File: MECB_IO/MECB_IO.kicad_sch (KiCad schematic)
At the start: 37 parts, among them J1 MECB_64AC, J2 Conn_02x10_Odd_Even, J3 Conn_01x03, SW1 SW_DIP_x08, U1 ATF22V10C-15PU, U2 74LS174, U3 DS1302+, U4 74LS245, U5 74LS374, Y1 32.768kHz

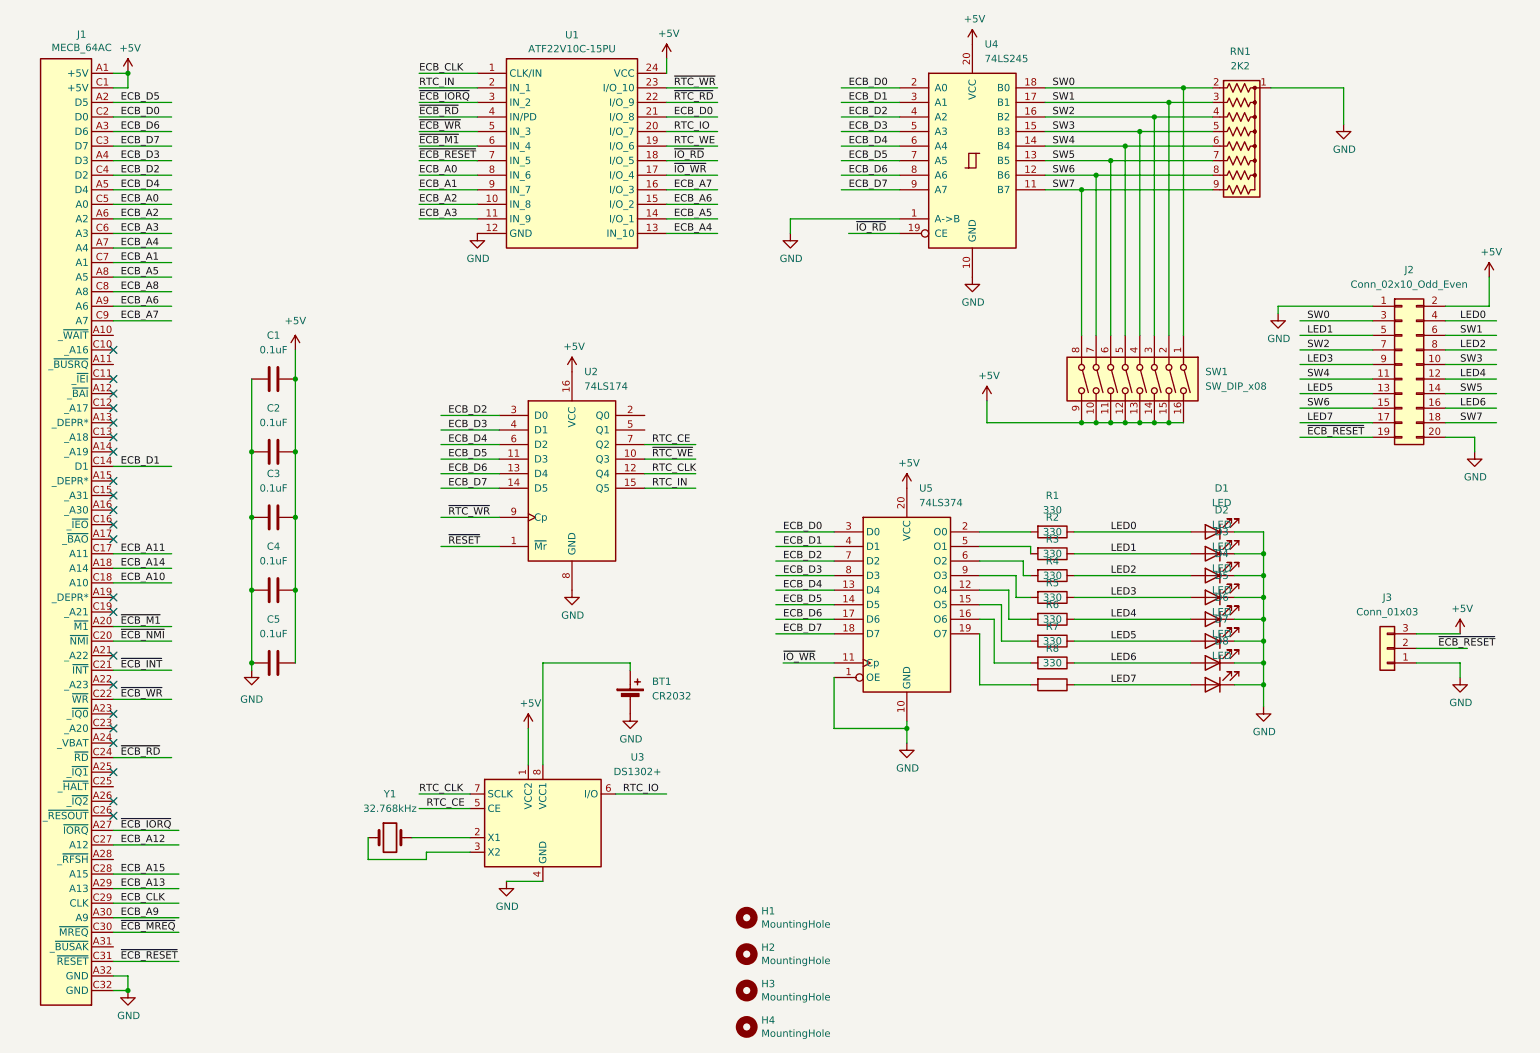
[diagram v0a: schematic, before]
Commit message: V1.0 board should fix the RTC issue
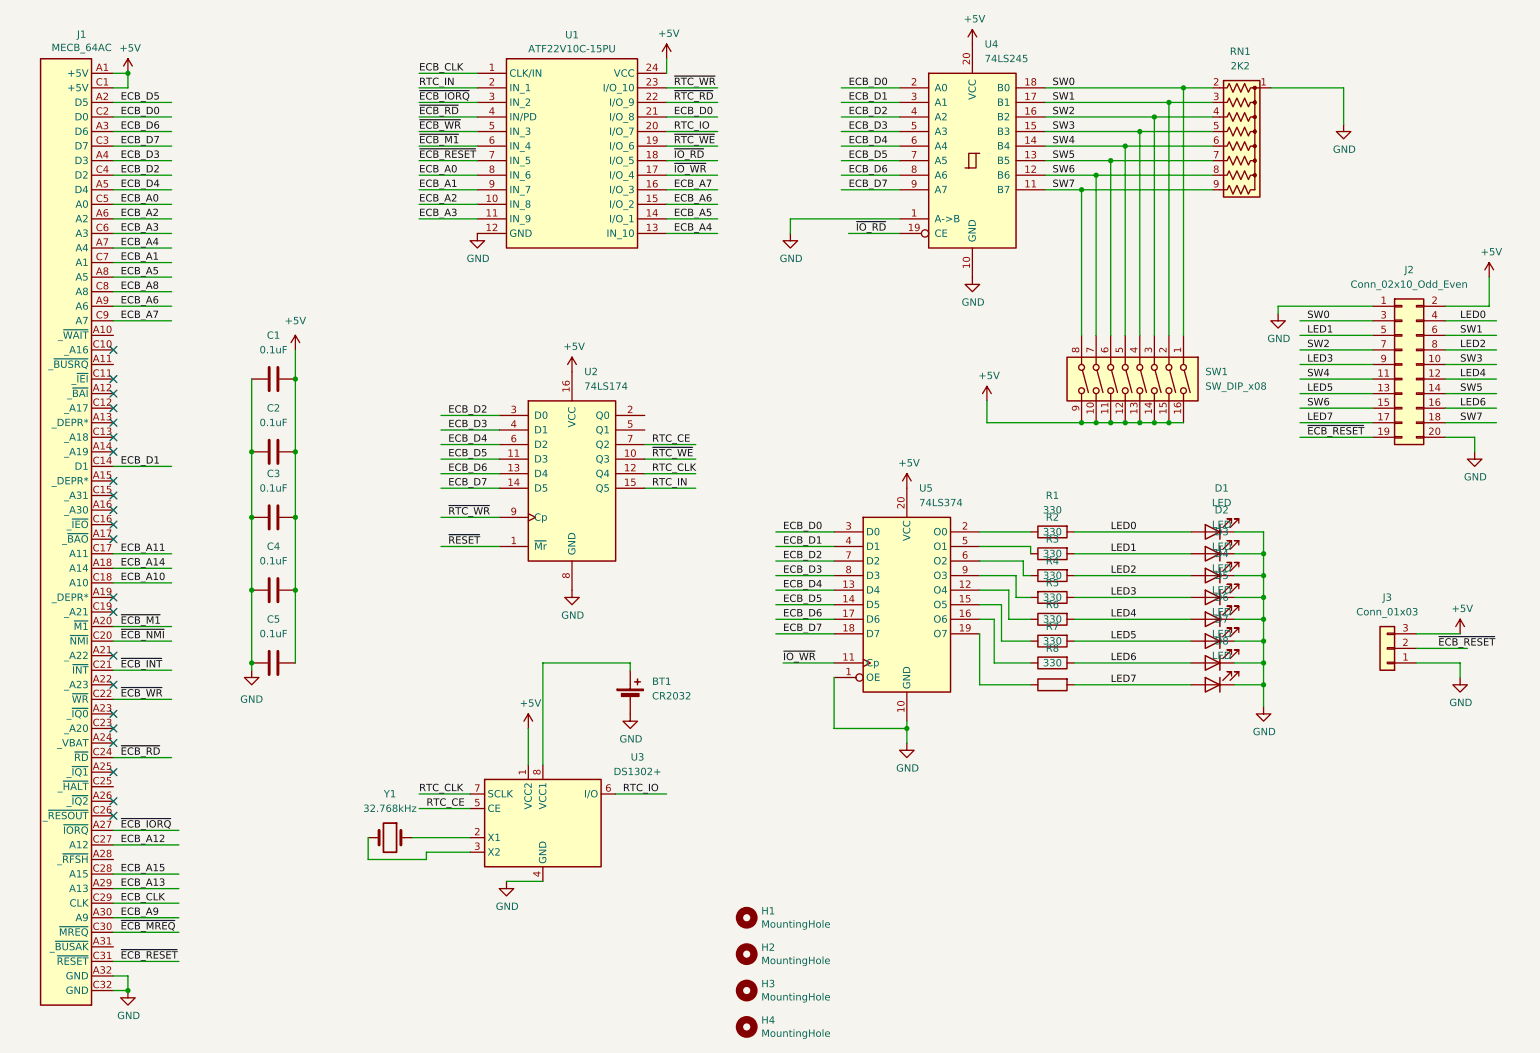
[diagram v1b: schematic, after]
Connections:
- net RTC_WE is gone; now on net ~{RTC_WE}: U1.19 (I/O_6)
- net LED0: now also R1.2; no longer R1.1
- net LED1: now also R2.2; no longer R2.1
- net LED2: now also R3.2; no longer R3.1
- net LED4: now also R5.2; no longer R5.1
- net LED5: now also R6.2; no longer R6.1
- net LED6: now also R7.2; no longer R7.1
- net LED7: now also R8.2; no longer R8.1
- net at U5.12 (O4): now also R5.1; no longer R5.2
- net at U5.19 (O7): now also R8.1; no longer R8.2
- net at U3.2 (X1): now also Y1.1; no longer Y1.2
- net at U3.3 (X2): now also Y1.2; no longer Y1.1
- net at U5.5 (O1): now also R2.1; no longer R2.2
- net at U5.6 (O2): now also R3.1; no longer R3.2
- net at U5.15 (O5): now also R6.1; no longer R6.2
- net at U5.16 (O6): now also R7.1; no longer R7.2
- net at U5.2 (O0): now also R1.1; no longer R1.2
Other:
- moved on the sheet: R1, R2, R3, R5, R6, R7, R8
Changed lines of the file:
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@@
 		)
 	)
-	(label "RTC_WE"
+	(label "~{RTC_WE}"
 		(at 129.54 40.64 0)
 		(effects
@@
 	(symbol
 		(lib_id "Device:R")
-		(at 195.58 123.19 270)
+		(at 195.58 123.19 90)
+		(mirror x)
 		(unit 1)
 		(exclude_from_sim no)
@@
 		(on_board yes)
 		(dnp no)
-		(fields_autoplaced yes)
 		(property "Reference" "R5"
 			(at 195.58 116.84 90)
@@
 	(symbol
 		(lib_id "Device:R")
-		(at 195.58 134.62 270)
+		(at 195.58 134.62 90)
+		(mirror x)
 		(unit 1)
 		(exclude_from_sim no)
@@
 		(on_board yes)
 		(dnp no)
-		(fields_autoplaced yes)
 		(property "Reference" "R8"
 			(at 195.58 128.27 90)
@@
 		(on_board yes)
 		(dnp no)
-		(fields_autoplaced yes)
 		(property "Reference" "R4"
 			(at 195.58 113.03 90)
@@
 	(symbol
 		(lib_id "Device:R")
-		(at 195.58 111.76 270)
+		(at 195.58 111.76 90)
+		(mirror x)
 		(unit 1)
 		(exclude_from_sim no)
@@
 		(on_board yes)
 		(dnp no)
-		(fields_autoplaced yes)
 		(property "Reference" "R2"
 			(at 195.58 105.41 90)
@@
 	(symbol
 		(lib_id "Device:R")
-		(at 195.58 115.57 270)
+		(at 195.58 115.57 90)
+		(mirror x)
 		(unit 1)
 		(exclude_from_sim no)
@@
 		(on_board yes)
 		(dnp no)
-		(fields_autoplaced yes)
 		(property "Reference" "R3"
 			(at 195.58 109.22 90)
@@
 	(symbol
 		(lib_id "Device:R")
-		(at 195.58 107.95 270)
+		(at 195.58 107.95 90)
+		(mirror x)
 		(unit 1)
 		(exclude_from_sim no)
@@
 		(on_board yes)
 		(dnp no)
-		(fields_autoplaced yes)
 		(property "Reference" "R1"
 			(at 195.58 101.6 90)
@@
 	(symbol
 		(lib_id "Device:R")
-		(at 195.58 127 270)
+		(at 195.58 127 90)
+		(mirror x)
 		(unit 1)
 		(exclude_from_sim no)
@@
 		(on_board yes)
 		(dnp no)
-		(fields_autoplaced yes)
 		(property "Reference" "R6"
 			(at 195.58 120.65 90)
@@
 		(lib_id "Device:Crystal")
 		(at 80.01 161.29 0)
+		(mirror y)
 		(unit 1)
 		(exclude_from_sim no)
@@
 		(on_board yes)
 		(dnp no)
-		(fields_autoplaced yes)
 		(property "Reference" "Y1"
 			(at 80.01 153.67 0)
@@
 	(symbol
 		(lib_id "Device:R")
-		(at 195.58 130.81 270)
+		(at 195.58 130.81 90)
+		(mirror x)
 		(unit 1)
 		(exclude_from_sim no)
@@
 		(on_board yes)
 		(dnp no)
-		(fields_autoplaced yes)
 		(property "Reference" "R7"
 			(at 195.58 124.46 90)
